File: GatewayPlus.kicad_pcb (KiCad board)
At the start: 2 copper layers, 100 x 60 mm, 140 parts, among them J1 LTDC_LCD_FPC_40p, J2 Micro_SD_Card, J3 ESP Anten, J4 xAnt, J5 HR911105A, SW1 SW_Push, SW2 ESP_RESET, SW3 ESP_BOOT, U1 STM32F429IGTx, U2 IS42S16400J - HY57V641620E, U3 W25Q128JVS, U4 ESP32-D0WD-V3, U5 W25Q32JVSS, U6 Ai-Thinker-Ra-02, U7 LAN8720A, X1 50MHz, Y1 32.768KHz, Y2 25MHz, Y3 40MHz

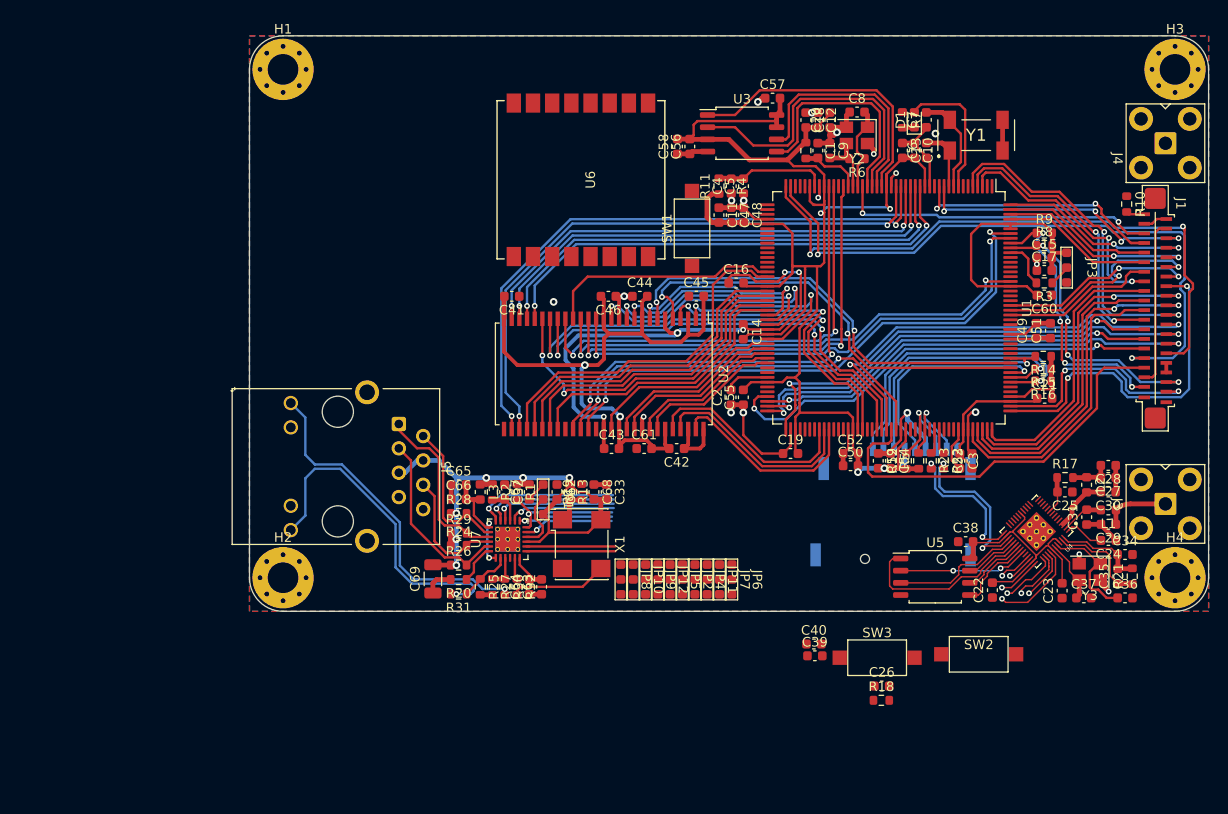
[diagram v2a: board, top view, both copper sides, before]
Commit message: Finish Ethernet Layout.
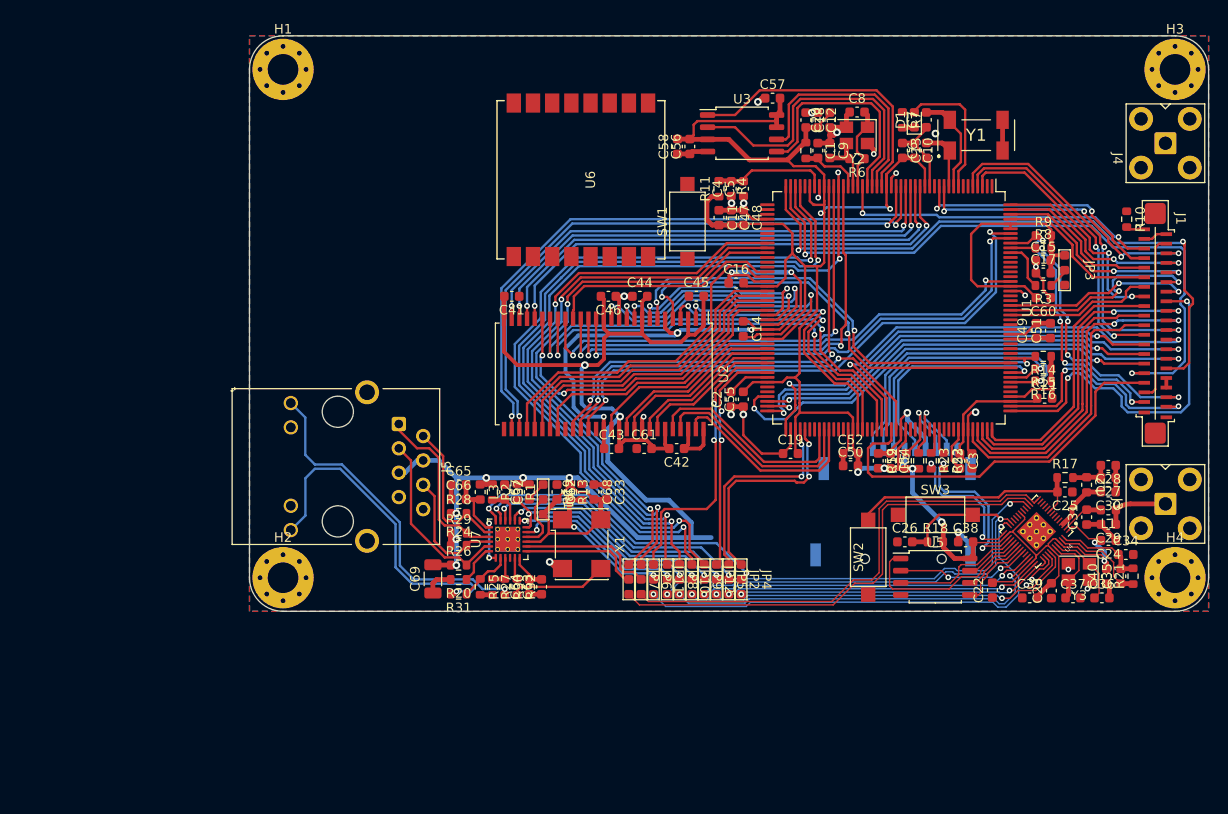
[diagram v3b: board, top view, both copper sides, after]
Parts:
- moved C40 31.3 mm to (189.3, 106.3), turned to 90 degrees
- moved C39 23.2 mm to (181.3, 108.6)
- moved R18 17.5 mm to (171.5, 102.8)
- moved SW3 16.1 mm to (171.5, 99.9)
- moved SW2 15.3 mm to (164.5, 104.4), turned to 90 degrees
- moved C26 15.2 mm to (168.3, 102.8)
- moved JP6 9.46 mm to (140.8, 106.7)
- moved JP7 9.46 mm to (139.6, 106.7)
- moved JP11 5.60 mm to (142.1, 106.7)
- moved JP10 4.83 mm to (144.8, 106.7)
- moved JP4 4.83 mm to (151.3, 106.7)
- moved JP8 4.83 mm to (143.6, 106.7)
- moved JP12 4.83 mm to (147.4, 106.7)
- moved JP2 4.83 mm to (150.0, 106.7)
- moved JP5 4.83 mm to (148.7, 106.7)
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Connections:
- C33 pad 2: +3V3 -> +3.3V
- C62 pad 2: +3V3 -> +3.3V
- C67 pad 2: +3V3 -> +3.3V
- C68 pad 2: +3V3 -> +3.3V
- C69 pad 2: +3V3 -> +3.3V
- J5 pad 4: +3V3 -> +3.3V
- J5 pad 5: +3V3 -> +3.3V
- JP1 pad 3: +3V3 -> +3.3V
- JP10 pad 1: unconnected-(JP10-Pad1) -> /MCU/RMII_MDC
- JP11 pad 1: unconnected-(JP11-Pad1) -> /MCU/ETH_CLKEN
- JP12 pad 1: unconnected-(JP12-Pad1) -> /MCU/ETH_REFCLK
- JP2 pad 1: unconnected-(JP2-Pad1) -> /MCU/RMII_TXD0
- JP4 pad 1: unconnected-(JP4-Pad1) -> /MCU/RMII_TXD1
- JP5 pad 1: unconnected-(JP5-Pad1) -> /MCU/RMII_TXEN
- JP6 pad 1: unconnected-(JP6-Pad1) -> /MCU/RMII_RXD0
- JP7 pad 1: unconnected-(JP7-Pad1) -> /MCU/RMII_RXD1
- JP8 pad 1: unconnected-(JP8-Pad1) -> /MCU/RMII_CRS_DV
- JP9 pad 1: unconnected-(JP9-Pad1) -> /MCU/RMII_MDIO
- L3 pad 1: +3V3 -> +3.3V
- R1 pad 1: +3V3 -> +3.3V
- R13 pad 1: +3V3 -> +3.3V
- R2 pad 1: +3V3 -> +3.3V
- R24 pad 1: +3V3 -> +3.3V
- R26 pad 1: +3V3 -> +3.3V
- R28 pad 1: +3V3 -> +3.3V
- R29 pad 1: +3V3 -> +3.3V
- U1 pad 33: unconnected-(U1-Pad33) -> /MCU/RMII_MDC
- U1 pad 41: unconnected-(U1-Pad41) -> /MCU/ETH_REFCLK
- U1 pad 42: unconnected-(U1-Pad42) -> /MCU/RMII_MDIO
- U1 pad 53: unconnected-(U1-Pad53) -> /MCU/RMII_CRS_DV
- U1 pad 54: unconnected-(U1-Pad54) -> /MCU/RMII_RXD0
- U1 pad 55: unconnected-(U1-Pad55) -> /MCU/RMII_RXD1
- U1 pad 79: unconnected-(U1-Pad79) -> /MCU/ETH_CLKEN
- U1 pad 80: unconnected-(U1-Pad80) -> /MCU/RMII_TXEN
- U1 pad 92: unconnected-(U1-Pad92) -> /MCU/RMII_TXD0
- U1 pad 93: unconnected-(U1-Pad93) -> /MCU/RMII_TXD1
- U7 pad 9: +3V3 -> +3.3V
- X1 pad 4: +3V3 -> +3.3V
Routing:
- net +3.3V: track 328.1 -> 450.9 mm, vias 7 -> 17
- net /MCU/ETH_REFCLK: track 0.00 -> 80.1 mm, vias 0 -> 2
- net /MCU/RMII_MDC: track 0.00 -> 79.3 mm, vias 0 -> 3
- net /MCU/RMII_MDIO: track 0.00 -> 78.7 mm, vias 0 -> 2
- net /MCU/RMII_CRS_DV: track 0.00 -> 61.6 mm, vias 0 -> 2
- net /MCU/RMII_RXD0: track 0.00 -> 60.9 mm, vias 0 -> 2
- net +3V3: track 60.3 -> 0.00 mm, vias 6 -> 0
- net /MCU/RMII_RXD1: track 0.00 -> 58.2 mm, vias 0 -> 2
- net /WIFI ESP32/RMII_RXD1: track 0.00 -> 51.1 mm
- net /WIFI ESP32/RMII_RXD0: track 0.00 -> 50.7 mm
- net /WIFI ESP32/ETH_REFCLK: track 0.00 -> 49.9 mm, vias 0 -> 2
- net /WIFI ESP32/ETH_CLKEN: track 0.00 -> 48.6 mm, vias 0 -> 2
- net /WIFI ESP32/RMII_CRSDV: track 0.00 -> 44.7 mm, vias 0 -> 2
- net /WIFI ESP32/RMII_MDC: track 2.84 -> 41.1 mm, vias 1 -> 2
- net /WIFI ESP32/RMII_MDIO: track 3.55 -> 37.4 mm, vias 1 -> 2
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
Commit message: Add RS485 Layout.
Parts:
- added C70: 10uF, Capacitor_SMD:C_1206_3216Metric, F.Cu at (173.8, 100.8)
- added C71: C_Small, Capacitor_SMD:C_0603_1608Metric, F.Cu at (118.5, 85.3)
- added D2: LED_WIFI, LED_SMD:LED_0603_1608Metric, F.Cu at (168.3, 100.2)
- added D3: RS_Tx, LED_SMD:LED_0603_1608Metric, F.Cu at (130.0, 92.9)
- added D4: RS_Rx, LED_SMD:LED_0603_1608Metric, F.Cu at (127.0, 92.9)
- added D5: D_TVS, Diode_SMD:D_SMA, F.Cu at (116.4, 71.2)
- added D6: D_TVS, Diode_SMD:D_SMA, F.Cu at (116.4, 74.7)
- added D7: D_TVS, Diode_SMD:D_SMA, F.Cu at (121.8, 72.9)
- added F1: Fuse, Fuse:Fuse_1812_4532Metric, F.Cu at (117.8, 82.3)
- added F2: Fuse, Fuse:Fuse_1812_4532Metric, F.Cu at (117.8, 78.4)
- added J6: RS485, TerminalBlock_Phoenix:TerminalBlock_Phoenix_MKDS-1,5-3-5.08_1x03_P5.08mm_Horizontal, F.Cu at (107.2, 72.4)
- added R33: R_Small, Resistor_SMD:R_0603_1608Metric, F.Cu at (168.3, 101.5)
- added R34: R_Small, Resistor_SMD:R_0603_1608Metric, F.Cu at (130.0, 94.3)
- added R35: R_Small, Resistor_SMD:R_0603_1608Metric, F.Cu at (127.0, 94.3)
- added R36: R_Small, Resistor_SMD:R_0603_1608Metric, F.Cu at (122.1, 93.6)
- added R37: R_Small, Resistor_SMD:R_0603_1608Metric, F.Cu at (123.4, 93.6)
- added R38: R_Small, Resistor_SMD:R_0603_1608Metric, F.Cu at (124.8, 93.6)
- added R39: R_Small, Resistor_SMD:R_0603_1608Metric, F.Cu at (120.8, 93.6)
- added R40: R_Small, Resistor_SMD:R_0603_1608Metric, F.Cu at (115.5, 85.3)
- added R41: R_Small, Resistor_SMD:R_0603_1608Metric, F.Cu at (122.3, 77.2)
- added R42: 120, Resistor_SMD:R_0805_2012Metric, F.Cu at (113.9, 80.4)
- added U8: MAX3485, Package_SO:SOIC-8_3.9x4.9mm_P1.27mm, F.Cu at (122.8, 88.3)
- moved SW3 8.09 mm to (164.7, 104.4), turned to 90 degrees
- moved SW2 3.92 mm to (160.6, 104.4)
- moved C28 2.93 mm to (187.0, 93.3), turned to -135 degrees
- moved C27 2.23 mm to (188.1, 94.4), turned to -135 degrees
- moved C30 2.15 mm to (189.1, 95.4), turned to -135 degrees
- moved L2 1.92 mm to (186.0, 95.4), turned to -45 degrees
- moved L1 1.66 mm to (188.1, 98.6), turned to -135 degrees
- moved C29 1.63 mm to (190.3, 99.5), turned to -90 degrees
- moved R17 1.27 mm to (183.8, 96.5), turned to 45 degrees
- moved C31 0.61 mm to (187.0, 100.7), turned to 135 degrees
- moved C25 0.13 mm to (184.9, 97.5), turned to -135 degrees
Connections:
- U4 pad 22: unconnected-(U4-Pad22) -> Net-(D2-Pad2)
- U6 pad 12: unconnected-(U6-Pad12) -> /RF-LORA-ZIGBEE/RF_SCK
- U6 pad 13: unconnected-(U6-Pad13) -> /RF-LORA-ZIGBEE/RF_MISO
- U6 pad 14: unconnected-(U6-Pad14) -> /RF-LORA-ZIGBEE/RF_MOSI
- U6 pad 15: unconnected-(U6-Pad15) -> /RF-LORA-ZIGBEE/RF_CS
- U6 pad 4: unconnected-(U6-Pad4) -> /RF-LORA-ZIGBEE/RF_RESET
- U6 pad 5: unconnected-(U6-Pad5) -> /RF-LORA-ZIGBEE/RF_IRQ
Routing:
- net Net-(D5-Pad1): track 0.00 -> 23.9 mm
- net Net-(D6-Pad1): track 0.00 -> 17.6 mm
- net Net-(C1-Pad2): track 6.55 -> 20.0 mm, vias 0 -> 2
- net Net-(D2-Pad2): track 0.00 -> 11.6 mm
- net /RS485/A+: track 0.00 -> 9.78 mm
- net /RS485/B-: track 0.00 -> 9.53 mm
- net /WIFI ESP32/ETH_REFCLK: track 49.9 -> 59.1 mm
- net +3.3V: track 450.9 -> 460.0 mm
- net Net-(C30-Pad2): track 6.18 -> 0.35 mm
- net /RS485/Tx: track 0.00 -> 5.10 mm
- net /RS485/Rx: track 0.00 -> 4.72 mm
- net Net-(R36-Pad2): track 0.00 -> 3.34 mm
- net Net-(R37-Pad2): track 0.00 -> 3.28 mm
- net Net-(C25-Pad2): track 25.2 -> 27.8 mm
- net Net-(D4-Pad1): track 0.00 -> 2.23 mm
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- added copper zone on F.Cu, net (none)
- added copper zone on F.Cu, net Net-(C29-Pad1)
- added copper zone on F.Cu, net Net-(C30-Pad2)
